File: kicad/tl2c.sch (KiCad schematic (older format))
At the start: 32 parts, among them IC101 ATTINY20-X, P101 12VDC, P102 I2C Master, P103 Spare, P104 ISP Header, P105 LED_DRIVER, P106 240VAC, P107 LED_DRIVER, P108 LED_OUT, SW101 TL3315NF160Q

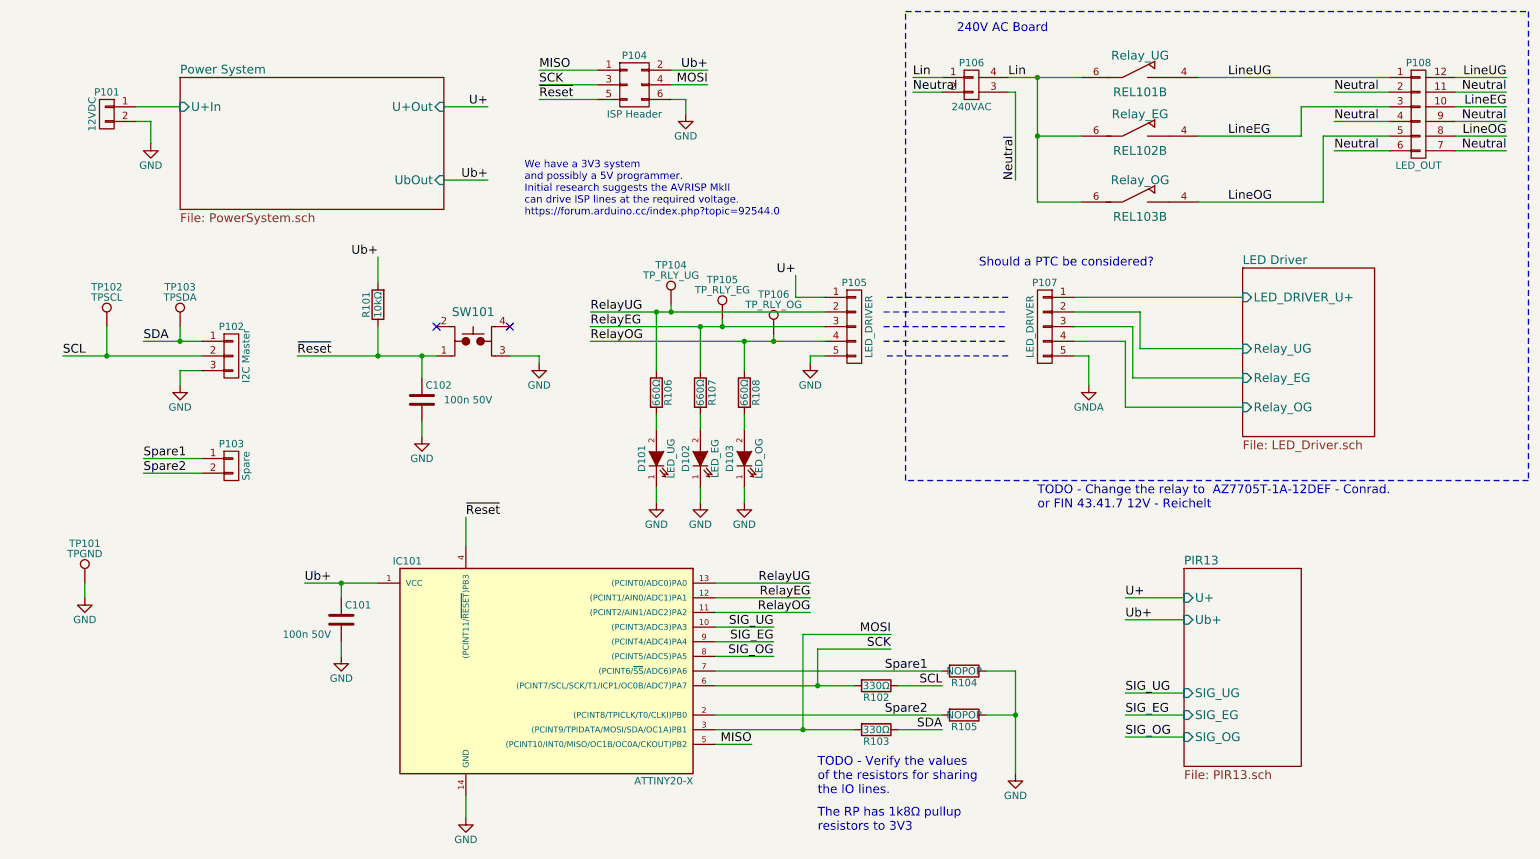
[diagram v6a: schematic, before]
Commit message: Included a small fuse on the Active. Finalised the board
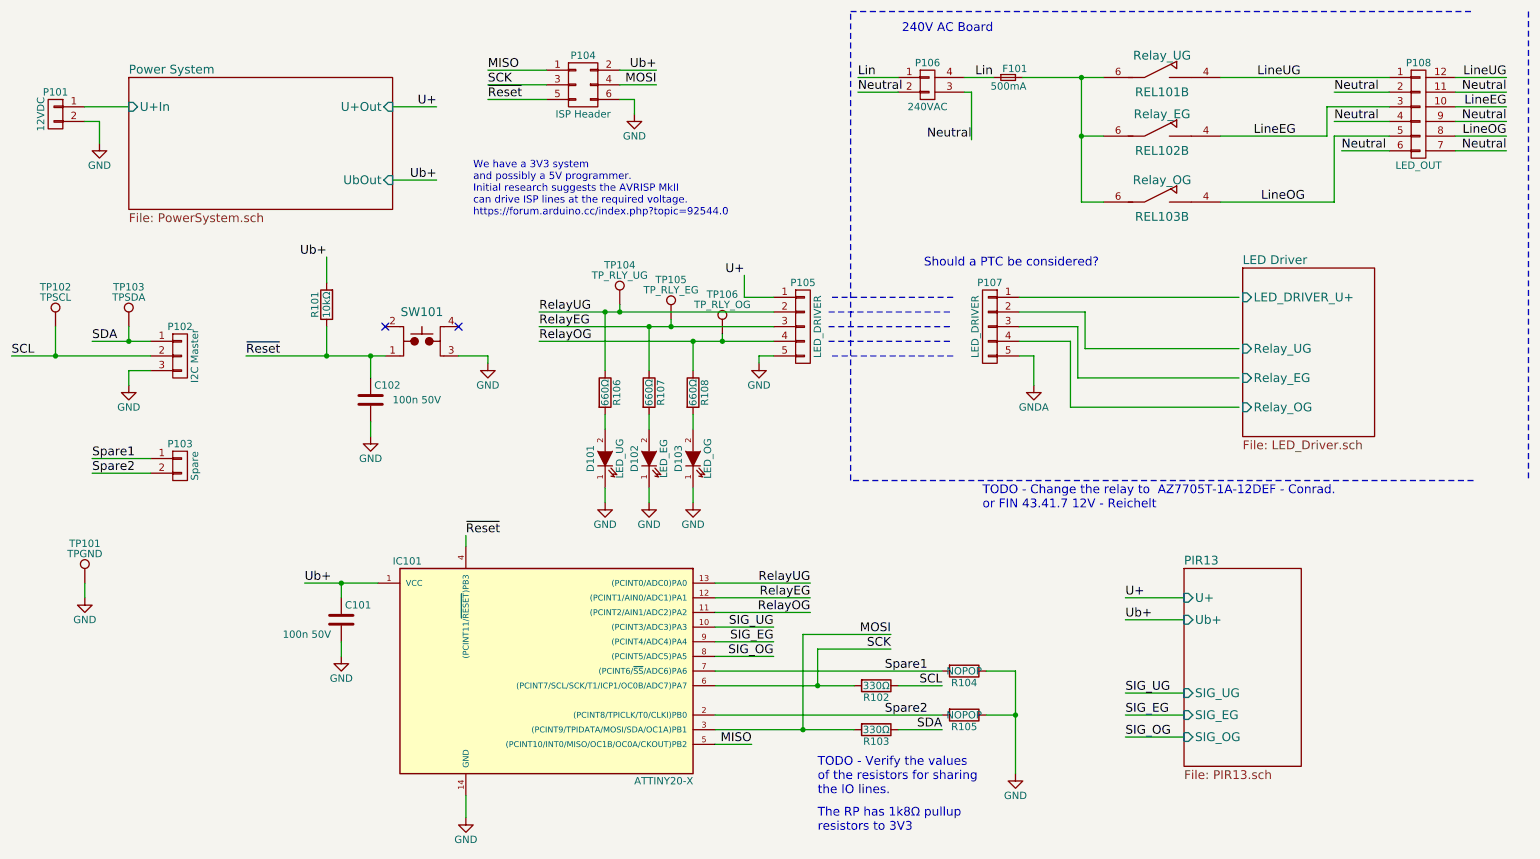
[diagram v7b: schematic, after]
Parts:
- added F101: 500mA, tl2c-footprint:Fuse_TE5_Littlefuse-ESKA_887_O14, symbol F_Small
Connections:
- net LED Driver/LED_DRIVER_U+: no longer P107.1 (P1)
- net LED Driver/Relay_EG: no longer P107.3 (P3)
- net LED Driver/Relay_OG: no longer P107.4 (P4)
- net LED Driver/Relay_UG: no longer P107.2 (P2)
- net Lin: now also F101.1; no longer REL101.6, REL102.6, REL103.6
- new net: F101.2, REL101.6, REL102.6, REL103.6
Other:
- moved on the sheet: C102, D101, D102, D103, P101, P102, P103, P104, P105, P106, P107, R101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

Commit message: Added the Reichelt-PN to the fuse for the last commit
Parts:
- F101: Reichelt-PN (none) -> MIK-FLINK 0,5A
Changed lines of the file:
@@
 F 5 "Value" H 7400 1150 60  0001 C CNN "Conrad-PN"
 F 6 "Value" H 7400 1150 60  0001 C CNN "Digikey-PN"
+F 7 "MIK-FLINK 0,5A" H 7400 1150 60  0001 C CNN "Reichelt-PN"
 	1    7400 1150
 	1    0    0    -1
